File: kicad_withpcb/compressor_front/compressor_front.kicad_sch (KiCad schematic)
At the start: 33 parts, among them J1 MAIN BOARD, SW1 BYPASS, SW2 INT/EXT, SW3 HPF DEFEAT, SW4 LINK, U10 LM3915, U9 LM3914

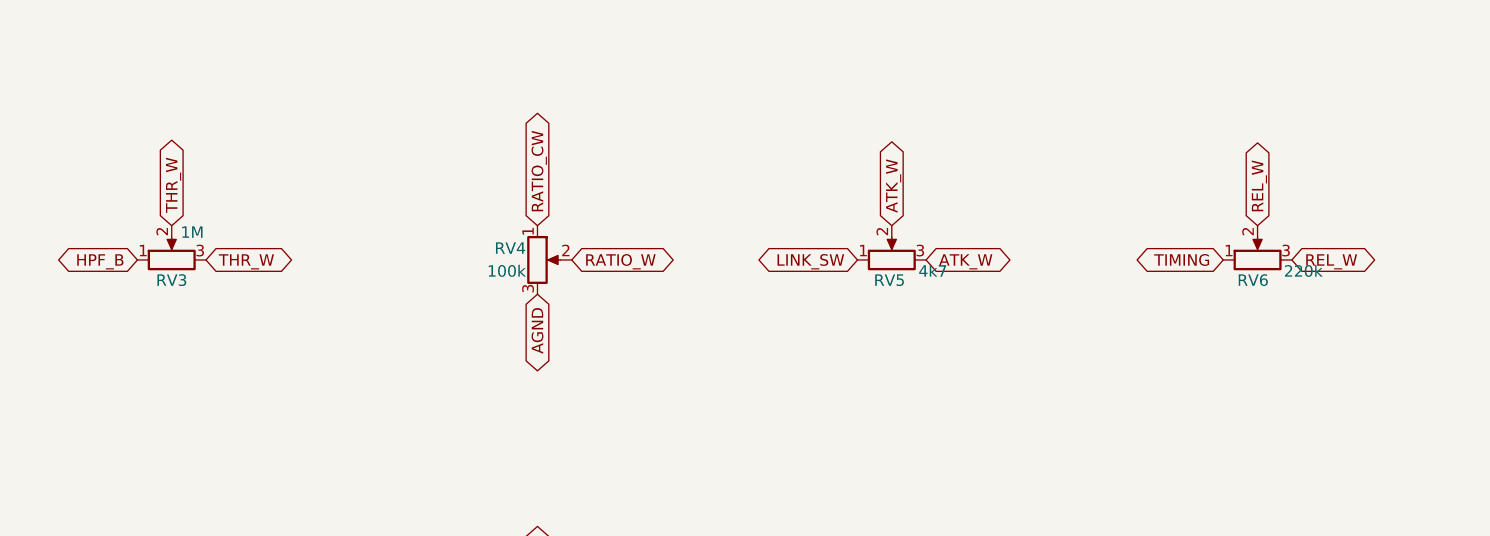
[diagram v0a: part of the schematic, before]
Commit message: Simulate the compressor, fix its values, and fit Altronics parts (#5)
* Make the schematic simulate in KiCad, and add the simulation results

Every part on the kicad/ sheets now has a SPICE model (Sim.* fields, models in
kicad/sim/compressor_models.lib), the connectors are excluded from simulation, and the
root sheet carries a test bench: the rack's supplies, a balanced source, a load and the
knob settings as .param lines. The netlist is unchanged.

tools/add_sim_models.py writes the fields. tools/sim/run_all.py exports the netlist with
kicad-cli and runs the characterisation in ngspice; kicad/sim/README.md has how to run
it in KiCad and what it found.

* Bring the compressor's values in line with the design targets

Through gain: R21/R22 3k3 to 6k8 halves the recovery amp's gain, so the
module is unity balanced in to out and BYPASS matches; R36 100k to 200k
keeps the detector's level. Bass: C9/C10 2u2 to 4u7 with the larger
input resistors puts the -3 dB point near 5 Hz.
Threshold: RV3 1M linear to 250k audio taper and R35 20k to 2k4 spread
about -20 to +20 dBu over the knob. R60 47k to 24k sets the resting
steer near 150 mV.
Timing: R45/R46/RV5 and R47/RV6/R74 scaled up to match the RC targets
with the same C15.

Same changes on the sheets, both boards and design.py. The simulation's
pot model gains an audio taper, and the burst test now runs at half
threshold.

* Carry the new values onto both boards' schematics and layouts

* Retune attack and release: R45 220R, R46 47R, RV5 10k, R47 15k

The first pass ran the attack too slow (9 to 103 ms against a 2.7 to
50 ms target). Results are regenerated in the next commit.

* Regenerate the simulation results for the new values

* Stop the fast-attack overshoot: C22 47u to 4u7

C22 made STA lag STB by about 60 ms, so when CTRL-B pulled the
reference node down the steering kept moving after the control
voltage had settled, overshooting by up to 20 dB. With 4u7 the two
sides track and the overshoot is about 1 dB. RV5 back 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
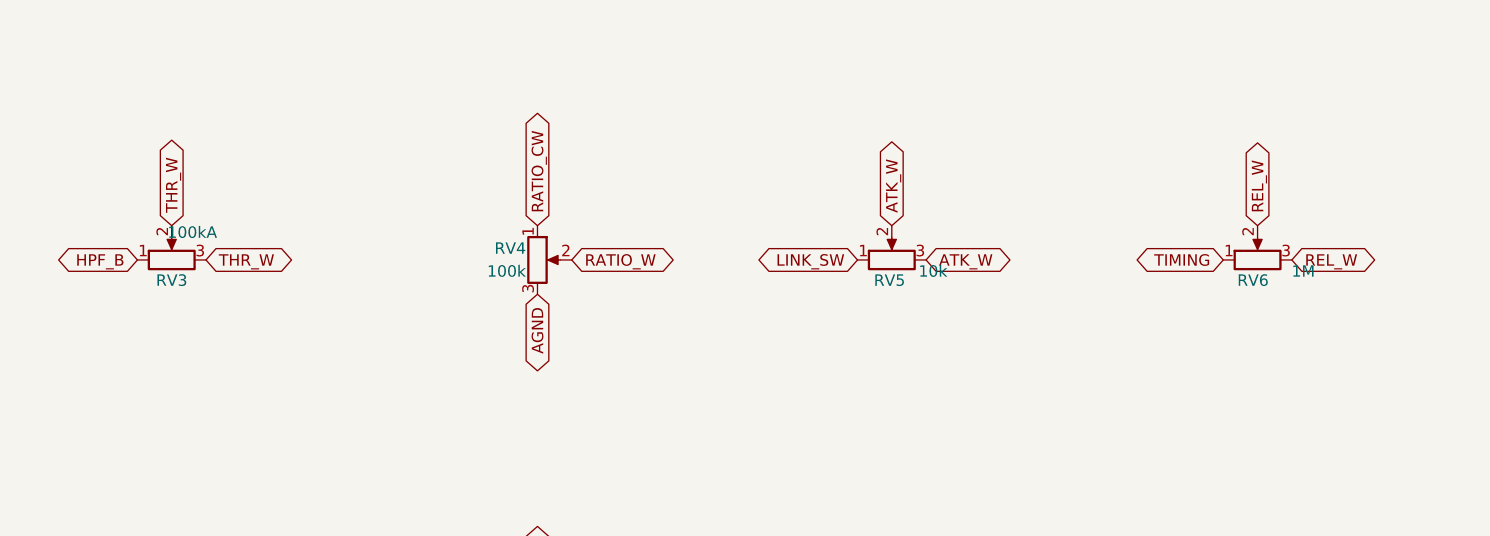
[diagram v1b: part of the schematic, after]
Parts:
- RV3: value 1M -> 100kA
- RV5: value 4k7 -> 10k
- RV6: value 220k -> 1M
- SW1: footprint compressor_front:SW_Toggle_SubMini_DPDT_Jaycar_ST0310 -> compressor_front:SW_Toggle_Mini_DPDT_Salecom_S1350
- SW2, SW3, SW4: footprint compressor_front:SW_Toggle_SubMini_SPDT_Jaycar_ST0300 -> compressor_front:SW_Toggle_Mini_SPDT_Salecom_S1315
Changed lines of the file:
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@@
 			)
 		)
-		(property "Value" "220k"
+		(property "Value" "1M"
 			(at 275.59 50.8 90)
 			(show_name no)
@@
 			)
 		)
-		(property "Footprint" "compressor_front:SW_Toggle_SubMini_SPDT_Jaycar_ST0300"
+		(property "Footprint" "compressor_front:SW_Toggle_Mini_SPDT_Salecom_S1315"
 			(at 277.622 104.14 0)
 			(hide yes)
@@
 			)
 		)
-		(property "Footprint" "compressor_front:SW_Toggle_SubMini_SPDT_Jaycar_ST0300"
+		(property "Footprint" "compressor_front:SW_Toggle_Mini_SPDT_Salecom_S1315"
 			(at 229.87 95.25 0)
 			(hide yes)
@@
 			)
 		)
-		(property "Footprint" "compressor_front:SW_Toggle_SubMini_SPDT_Jaycar_ST0300"
+		(property "Footprint" "compressor_front:SW_Toggle_Mini_SPDT_Salecom_S1315"
 			(at 190.5 95.25 0)
 			(hide yes)
@@
 			)
 		)
-		(property "Footprint" "compressor_front:SW_Toggle_SubMini_DPDT_Jaycar_ST0310"
+		(property "Footprint" "compressor_front:SW_Toggle_Mini_DPDT_Salecom_S1350"
 			(at 110.49 95.25 0)
 			(hide yes)
@@
 			)
 		)
-		(property "Value" "4k7"
+		(property "Value" "10k"
 			(at 234.442 50.8 90)
 			(show_name no)
@@
 			)
 		)
-		(property "Value" "1M"
+		(property "Value" "100kA"
 			(at 152.146 46.482 90)
 			(show_name no)
@@
 			)
 		)
-		(property "Footprint" "compressor_front:SW_Toggle_SubMini_DPDT_Jaycar_ST0310"
+		(property "Footprint" "compressor_front:SW_Toggle_Mini_DPDT_Salecom_S1350"
 			(at 149.86 95.25 0)
 			(hide yes)

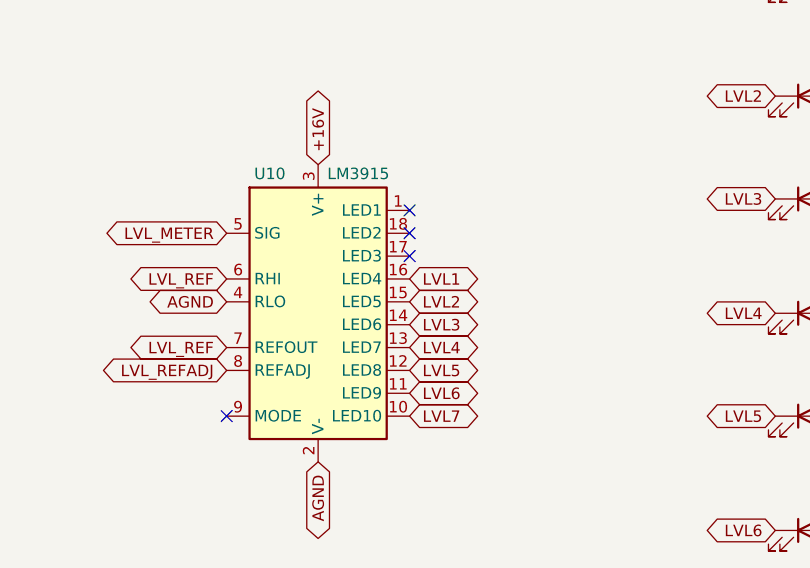
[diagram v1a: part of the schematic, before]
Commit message: Swap the level meter's LM3915 for an LM3914 on outputs 1-7
Nobody stocks the LM3915, so U10 becomes a second LM3914. The LEDs move
to outputs 1-7 and outputs 8-10 join the top LED, giving a 17 dB scale
with no added parts. Front board LVL tracks re-routed; BOM regenerated.
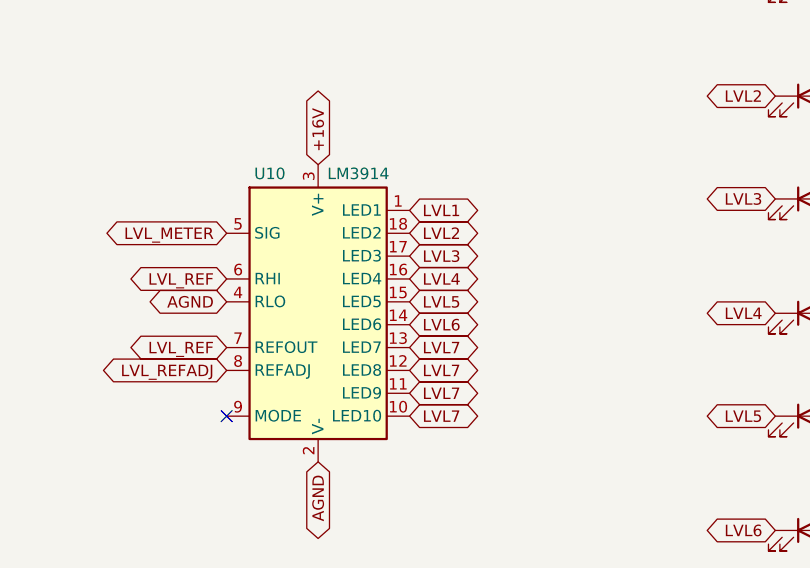
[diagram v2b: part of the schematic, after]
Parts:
- U10: value LM3915 -> LM3914
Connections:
- net LVL1: now also U10.1 (LED1); no longer U10.16 (LED4)
- net LVL2: now also U10.18 (LED2); no longer U10.15 (LED5)
- net LVL3: now also U10.17 (LED3); no longer U10.14 (LED6)
- net LVL4: now also U10.16 (LED4); no longer U10.13 (LED7)
- net LVL5: now also U10.15 (LED5); no longer U10.12 (LED8)
- net LVL6: now also U10.14 (LED6); no longer U10.11 (LED9)
- net LVL7: now also U10.11 (LED9), U10.12 (LED8), U10.13 (LED7)
- no-connect marks 8 -> 5
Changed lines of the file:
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@@
 			)
 		)
-		(property "Value" "LM3915"
+		(property "Value" "LM3914"
 			(at 271.526 155.956 0)
 			(show_name no)
@@
 		)
 	)
-	(no_connect
-		(at 280.67 160.02)
-	)
 	(global_label "AGND"
 		(shape bidirectional)
@@
 		)
 	)
+	(global_label "LVL7"
+		(shape bidirectional)
+		(at 280.67 180.34 0)
+		(fields_autoplaced yes)
+		(effects
+			(font
+				(size 1.27 1.27)
+			)
+			(justify left)
+		)
+		(property "Intersheetrefs" "${INTERSHEET_REFS}"
+			(at 280.67 180.34 0)
+			(hide yes)
+			(show_name no)
+			(do_not_autoplace no)
+			(effects
+				(font
+					(size 1.27 1.27)
+				)
+				(justify left)
+			)
+		)
+	)
+	(global_label "LVL7"
+		(shape bidirectional)
+		(at 280.67 177.8 0)
+		(fields_autoplaced yes)
+		(effects
+			(font
+				(size 1.27 1.27)
+			)
+			(justify left)
+		)
+		(property "Intersheetrefs" "${INTERSHEET_REFS}"
+			(at 280.67 177.8 0)
+			(hide yes)
+			(show_name no)
+			(do_not_autoplace no)
+			(effects
+				(font
+					(size 1.27 1.27)
+				)
+				(justify left)
+			)
+		)
+	)
+	(global_label "LVL7"
+		(shape bidirectional)
+		(at 280.67 175.26 0)
+		(fields_autoplaced yes)
+		(effects
+			(font
+				(size 1.27 1.27)
+			)
+			(justify left)
+		)
+		(property "Intersheetrefs" "${INTERSHEET_REFS}"
+			(at 280.67 175.26 0)
+			(hide yes)
+			(show_name no)
+			(do_not_autoplace no)
+			(effects
+				(font
+					(size 1.27 1.27)
+				)
+				(justify left)
+			)
+		)
+	)
 	(global_label "LVL6"
 		(shape bidirectional)
-		(at 280.67 180.34 0)
-		(fields_autoplaced yes)
-		(effects
-			(font
-				(size 1.27 1.27)
-			)
-			(justify left)
-		)
-		(property "Intersheetrefs" "${INTERSHEET_REFS}"
-			(at 280.67 180.34 0)
+		(at 280.67 172.72 0)
+		(fields_autoplaced yes)
+		(effects
+			(font
+				(size 1.27 1.27)
+			)
+			(justify left)
+		)
+		(property "Intersheetrefs" "${INTERSHEET_REFS}"
+			(at 280.67 172.72 0)
 			(hide yes)
 			(show_name no)
@@
 	(global_label "LVL5"
 		(shape bidirectional)
-		(at 280.67 177.8 0)
-		(fields_autoplaced yes)
-		(effects
-			(font
-				(size 1.27 1.27)
-			)
-			(justify left)
-		)
-		(property "Intersheetrefs" "${INTERSHEET_REFS}"
-			(at 280.67 177.8 0)
+		(at 280.67 170.18 0)
+		(fields_autoplaced yes)
+		(effects
+			(font
+				(size 1.27 1.27)
+			)
+			(justify left)
+		)
+		(property "Intersheetrefs" "${INTERSHEET_REFS}"
+			(at 280.67 170.18 0)
 			(hide yes)
 			(show_name no)
@@
 	(global_label "LVL4"
 		(shape bidirectional)
-		(at 280.67 175.26 0)
-		(fields_autoplaced yes)
-		(effects
-			(font
-				(size 1.27 1.27)
-			)
-			(justify left)
-		)
-		(property "Intersheetrefs" "${INTERSHEET_REFS}"
-			(at 280.67 175.26 0)
-			(hide yes)
-			(show_name no)
-			(do_not_autoplace no)
-			(effects
-				(font
-					(size 1.27 1.27)
-				)
-				(justify left)
-			)
-		)
-	)
-	(global_label "LVL3"
-		(shape bidirectional)
-		(at 280.67 172.72 0)
-		(fields_autoplaced yes)
-		(effects
-			(font
-				(size 1.27 1.27)
-			)
-			(justify left)
-		)
-		(property "Intersheetrefs" "${INTERSHEET_REFS}"
-			(at 280.67 172.72 0)
-			(hide yes)
-			(show_name no)
-			(do_not_autoplace no)
-			(effects
-				(font
-					(size 1.27 1.27)
-				)
-				(justify left)
-			)
-		)
-	)
-	(global_label "LVL2"
-		(shape bidirectional)
-		(at 280.67 170.18 0)
-		(fields_autoplaced yes)
-		(effects
-			(font
-				(size 1.27 1.27)
-			)
-			(justify left)
-		)
-		(property "Intersheetrefs" "${INTERSHEET_REFS}"
-			(at 280.67 170.18 0)
-			(hide yes)
-			(show_name no)
-			(do_not_autoplace no)
-			(effects
-				(font
-					(size 1.27 1.27)
-				)
-				(justify left)
-			)
-		)
-	)
-	(global_label "LVL1"
-		(shape bidirectional)
 		(at 280.67 167.64 0)
 		(fields_autoplaced yes)
@@
 			)
 		)
-	)
-	(no_connect
-		(at 280.67 165.1)
-	)
-	(no_connect
-		(at 280.67 162.56)
 	)
 		(symbol
@@
 		)
 	)
+	(global_label "LVL3"
+		(shape bidirectional)
+		(at 280.67 165.1 0)
+		(fields_autoplaced yes)
+		(effects
+			(font
+				(size 1.27 1.27)
+			)
+			(justify left)
+		)
+		(property "Intersheetrefs" "${INTERSHEET_REFS}"
+			(at 280.67 165.1 0)
+			(hide yes)
+			(show_name no)
+			(do_not_autoplace no)
+			(effects
+				(font
+					(size 1.27 1.27)
+				)
+				(justify left)
+			)
+		)
+	)
+	(global_label "LVL2"
+		(shape bidirectional)
+		(at 280.67 162.56 0)
+		(fields_autoplaced yes)
+		(effects
+			(font
+				(size 1.27 1.27)
+			)
+			(justify left)
+		)
+		(property "Intersheetrefs" "${INTERSHEET_REFS}"
+			(at 280.67 162.56 0)
+			(hide yes)
+			(show_name no)
+			(do_not_autoplace no)
+			(effects
+				(font
+					(size 1.27 1.27)
+				)
+				(justify left)
+			)
+		)
+	)
+	(global_label "LVL1"
+		(shape bidirectional)
+		(at 280.67 160.02 0)
+		(fields_autoplaced yes)
+		(effects
+			(font
+				(size 1.27 1.27)
+			)
+			(justify left)
+		)
+		(property "Intersheetrefs" "${INTERSHEET_REFS}"
+			(at 280.67 160.02 0)
+			(hide yes)
+			(show_name no)
+			(do_not_autoplace no)
+			(effects
+				(font
+					(size 1.27 1.27)
+				)
+				(justify left)
+			)
+		)
+	)
